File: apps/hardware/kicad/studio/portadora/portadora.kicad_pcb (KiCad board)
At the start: 2 copper layers, 0 parts

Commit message: feat(hardware): enclosure +15 mm, PCB-A de una cara y ubicación de la portadora
Enclosure (design/README.md, theory/02 §3 y §4.3–4.5), medido el módulo Freenove con la Pi:
- Cuña de 43/78 mm (+15 mm parejo, 12°): la portadora entra bajo la Pi con margen y hay más aire.
- Pantalla corrida 2.5 mm hacia atrás (centro y 114.9): el vidrio (120.8 × 76 × 7.6 mm) ya no se monta
  sobre PCB-K; ranuras de aire en y 155–165.
- Pi atornillada detrás de la Freenove, puertos hacia la derecha (adentro): se elimina la tapa de servicio.
- Jacks en una hilera baja soldados a la portadora (1/4" NRJ3HF-1); USB y palanca PAD de panel arriba.
  La placa trasera vertical se descartó antes de commit.

PCB-A: todos los SMD en la cara superior (ensamble Economic de una cara); vía propia para los GND del
JST; re-ruteada. DRC 0/0.

Portadora: tools/place_portadora.py (97 × 100 mm, jacks contra la pared, shield y entrada analógica al
medio, Teensy y alimentación adelante, J5/J6 al frente). DRC con paridad: 0 violaciones; falta rutear.
Herramientas: costura de GND que respeta agujeros e islas, route_board sin duplicar lo bloqueado,
sync_fp_fields con redes "unconnected" y atributos de BOM, trim_silk_outside.py.

Co-Authored-By: Claude Opus 5.5 <noreply@anthropic.com>
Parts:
- added C1: 100uF, Capacitor_SMD:CP_Elec_6.3x7.7, F.Cu at (178.0, 120.0)
- added C10: 10uF, Capacitor_SMD:C_0805_2012Metric, F.Cu at (185.0, 88.0)
- added C11: 10uF, Capacitor_SMD:C_0805_2012Metric, F.Cu at (147.0, 65.5)
- added C12: 10uF, Capacitor_SMD:C_0805_2012Metric, F.Cu at (129.0, 65.5)
- added C13: 100nF, Capacitor_SMD:C_0603_1608Metric, F.Cu at (103.0, 67.5)
- added C14: 100nF, Capacitor_SMD:C_0603_1608Metric, F.Cu at (107.0, 67.5)
- added C2: 100nF, Capacitor_SMD:C_0603_1608Metric, F.Cu at (148.0, 114.4)
- added C3: 10uF, Capacitor_SMD:C_0805_2012Metric, F.Cu at (171.0, 120.0)
- added C4: 100nF, Capacitor_SMD:C_0603_1608Metric, F.Cu at (186.0, 126.5)
- added C5: 1uF, Capacitor_SMD:C_0805_2012Metric, F.Cu at (150.0, 79.0)
- added C6: 1uF, Capacitor_SMD:C_0805_2012Metric, F.Cu at (150.0, 97.0)
- added C7: 100nF, Capacitor_SMD:C_0603_1608Metric, F.Cu at (168.0, 94.5)
- added C8: 2.2uF, Capacitor_SMD:C_0805_2012Metric, F.Cu at (176.0, 82.0)
- added C9: 2.2uF, Capacitor_SMD:C_0805_2012Metric, F.Cu at (176.0, 94.0)
- added D1: SMBJ5.0CA, Diode_SMD:D_SMB, F.Cu at (171.0, 112.0)
- added D2: BAT54S, Package_TO_SOT_SMD:SOT-23, F.Cu at (158.0, 79.0)
- added D3: BAT54S, Package_TO_SOT_SMD:SOT-23, F.Cu at (158.0, 97.0)
- added F1: 3A hold, Fuse:Fuse_1812_4532Metric, F.Cu at (177.0, 112.0)
- added J1: Teensy 4.1 izq, Connector_PinSocket_2.54mm:PinSocket_1x24_P2.54mm_Vertical, F.Cu at (101.3, 125.0)
- added J10: 5V desde USB-C de panel, Connector_JST:JST_XH_B2B-XH-A_1x02_P2.50mm_Vertical, F.Cu at (184.0, 112.0)
- added J11: OUT L 1/4 NRJ3HF-1, Connector_Audio:Jack_6.35mm_Neutrik_NRJ3HF-1_Horizontal, F.Cu at (139.8, 55.0)
- added J12: OUT R 1/4 NRJ3HF-1, Connector_Audio:Jack_6.35mm_Neutrik_NRJ3HF-1_Horizontal, F.Cu at (121.8, 55.0)
- added J13: PHONES 3.5 sleeve HP_VGND, Connector_Audio:Jack_3.5mm_CUI_SJ1-3533NG_Horizontal, F.Cu at (111.1, 39.2)
- added J14: CV OUT 3.5, Connector_Audio:Jack_3.5mm_CUI_SJ1-3533NG_Horizontal, F.Cu at (99.1, 39.2)
- added J15: Shield fila 13-5V, Connector_PinSocket_2.54mm:PinSocket_1x14_P2.54mm_Vertical, F.Cu at (106.5, 84.4)
- added J16: Shield fila 12-GND, Connector_PinSocket_2.54mm:PinSocket_1x14_P2.54mm_Vertical, F.Cu at (106.5, 99.6)
- added J2: Teensy 4.1 der, Connector_PinSocket_2.54mm:PinSocket_1x24_P2.54mm_Vertical, F.Cu at (101.3, 109.8)
- added J3: USB host Teensy, Connector_PinHeader_2.54mm:PinHeader_1x05_P2.54mm_Vertical, F.Cu at (96.5, 77.9)
- added J5: Panel IDC 2x15, Connector_IDC:IDC-Header_2x15_P2.54mm_Vertical, F.Cu at (144.2, 134.1)
- added J6: Raspberry Pi pines 1-10, Connector_IDC:IDC-Header_2x05_P2.54mm_Vertical, F.Cu at (101.9, 134.1)
- added J7: IN L 1/4 NRJ3HF-1, Connector_Audio:Jack_6.35mm_Neutrik_NRJ3HF-1_Horizontal, F.Cu at (175.8, 55.0)
- added J8: IN R 1/4 NRJ3HF-1, Connector_Audio:Jack_6.35mm_Neutrik_NRJ3HF-1_Horizontal, F.Cu at (157.8, 55.0)
- added J9: Audio Shield LINE y HP, Connector_PinHeader_2.54mm:PinHeader_1x09_P2.54mm_Vertical, F.Cu at (143.5, 83.6)
- added JP1: LED buffer o directo, Jumper:SolderJumper-3_P1.3mm_Bridged12_RoundedPad1.0x1.5mm, F.Cu at (153.0, 118.0)
- added JP2: BYP L (sin U2), Jumper:SolderJumper-2_P1.3mm_Open_RoundedPad1.0x1.5mm, F.Cu at (172.0, 78.5)
- added JP3: BYP R (sin U2), Jumper:SolderJumper-2_P1.3mm_Open_RoundedPad1.0x1.5mm, F.Cu at (172.0, 97.5)
- added JP4: BYP VREF (sin U2), Jumper:SolderJumper-2_P1.3mm_Open_RoundedPad1.0x1.5mm, F.Cu at (180.0, 96.0)
- added JP5: BYP CV (sin U2), Jumper:SolderJumper-2_P1.3mm_Open_RoundedPad1.0x1.5mm, F.Cu at (180.0, 80.0)
- added R10: 1k, Resistor_SMD:R_0603_1608Metric, F.Cu at (154.0, 79.0)
- added R11: 1k, Resistor_SMD:R_0603_1608Metric, F.Cu at (154.0, 97.0)
- added R12: 100k, Resistor_SMD:R_0603_1608Metric, F.Cu at (162.0, 79.0)
- added R13: 100k, Resistor_SMD:R_0603_1608Metric, F.Cu at (162.0, 97.0)
- added R14: 10k, Resistor_SMD:R_0603_1608Metric, F.Cu at (179.5, 88.0)
- added R15: 10k, Resistor_SMD:R_0603_1608Metric, F.Cu at (182.0, 88.0)
- added R16: 47k, Resistor_SMD:R_0603_1608Metric, F.Cu at (147.0, 68.5)
- added R17: 47k, Resistor_SMD:R_0603_1608Metric, F.Cu at (129.0, 68.5)
- added R18: 4.7k, Resistor_SMD:R_0603_1608Metric, F.Cu at (103.0, 65.0)
- added R19: 4.7k, Resistor_SMD:R_0603_1608Metric, F.Cu at (107.0, 65.0)
- added R20: 1k, Resistor_SMD:R_0603_1608Metric, F.Cu at (107.0, 70.0)
- added R3: 330, Resistor_SMD:R_0603_1608Metric, F.Cu at (157.0, 118.0)
- added R4: 32.4k, Resistor_SMD:R_0603_1608Metric, F.Cu at (183.0, 65.0)
- added R5: 12.4k, Resistor_SMD:R_0603_1608Metric, F.Cu at (183.0, 67.5)
- added R6: 5.23k, Resistor_SMD:R_0603_1608Metric, F.Cu at (183.0, 70.0)
- added R7: 32.4k, Resistor_SMD:R_0603_1608Metric, F.Cu at (165.0, 65.0)
- added R8: 12.4k, Resistor_SMD:R_0603_1608Metric, F.Cu at (165.0, 67.5)
- added R9: 5.23k, Resistor_SMD:R_0603_1608Metric, F.Cu at (165.0, 70.0)
- added SW1: PAD 0 -10 -20 dB, Connector_PinHeader_2.54mm:PinHeader_2x04_P2.54mm_Vertical, F.Cu at (172.7, 64.7)
- added TP1: VREF, TestPoint:TestPoint_Pad_D1.5mm, F.Cu at (187.0, 94.0)
- added TP2: BUF_L, TestPoint:TestPoint_Pad_D1.5mm, F.Cu at (187.0, 82.0)
- added TP3: BUF_R, TestPoint:TestPoint_Pad_D1.5mm, F.Cu at (187.0, 100.0)
- added TP4: CV_BUF, TestPoint:TestPoint_Pad_D1.5mm, F.Cu at (187.0, 76.0)
- added TP5: GND, TestPoint:TestPoint_Pad_D1.5mm, F.Cu at (147.8, 88.0)
- added U1: 74AHCT1G125, Package_TO_SOT_SMD:SOT-23-5, F.Cu at (148.0, 118.0)
- added U2: MCP6004, Package_SO:SOIC-14_3.9x8.7mm_P1.27mm, F.Cu at (168.0, 88.0)
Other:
- board outline added: 97 x 100 mm

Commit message: feat(hardware): portadora ruteada (DRC limpio) y pinout del IDC reordenado
- Portadora: ruteo completo, DRC con paridad de esquemático 0/0/0 contra reglas de JLCPCB.
  +5V de F1 a la Pi en ~40 mm con una vía; sin paralelos audio↔digital a <1 mm.
- IDC 2×15 (PCB-A J2 ↔ portadora J5): pines ordenados por la X del pin de la Teensy al que van,
  para que el bus salga del conector sin cruces. Ambos esquemáticos re-etiquetados (ERC limpio),
  PCB-A re-ruteada (DRC 0/0/0). Tablas y razón en theory/02 §6.2.
- Herramientas: grid_route (Dijkstra en grilla 0.1 mm, 2 capas), finish_routing (rip-up and
  reroute de lo que deja Freerouting), clean_vias, add_gnd_escapes, fix_portadora_gnd,
  set_idc_pinout y build_portadora.sh (pipeline completo reproducible).

Co-Authored-By: Claude Opus 5.5 <noreply@anthropic.com>
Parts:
- moved J10 65.6 mm to (122.0, 133.5)
- moved C3 51.2 mm to (120.5, 128.4), turned to 0 degrees
- moved F1 50.2 mm to (132.5, 135.2), turned to 0 degrees
- moved D1 42.4 mm to (132.8, 130.4), turned to 0 degrees
- moved C1 2.00 mm to (178.0, 118.0)
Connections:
- J5 pad 11: /B5 -> /NAV_B
- J5 pad 12: /B6 -> /NAV_A
- J5 pad 13: /ENCL_A -> /P2_SW
- J5 pad 14: /ENCL_B -> /ENCR_SW
- J5 pad 15: /ENCL_SW -> /ENCL_A
- J5 pad 16: /ENCR_A -> /ENCR_B
- J5 pad 17: /ENCR_B -> /ENCL_B
- J5 pad 18: /ENCR_SW -> /ENCR_A
- J5 pad 19: /NAV_A -> /ENCL_SW
- J5 pad 20: /NAV_B -> /B6
- J5 pad 21: /NAV_SW -> /POT_IN
- J5 pad 22: /P1_A -> /B5
- J5 pad 23: /P1_B -> /NAV_SW
- J5 pad 24: /P1_SW -> /P2_B
- J5 pad 25: /P2_A -> /P1_A
- J5 pad 26: /P2_B -> /LED_DIN
- J5 pad 27: /P2_SW -> /P2_A
- J5 pad 28: /POT_IN -> /P1_B
- J5 pad 29: /POT_VOL -> /P1_SW
- J5 pad 5: /LED_DIN -> /B1
- J5 pad 7: /B1 -> /B2
- J5 pad 8: /B2 -> /POT_VOL
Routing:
- net /+3V3: track 0.00 -> 200.0 mm, vias 0 -> 2
- net /+5V: track 0.00 -> 164.2 mm, vias 0 -> 3
- net /CV_BUF: track 0.00 -> 105.6 mm, vias 0 -> 2
- net /GND: track 0.00 -> 104.8 mm, vias 0 -> 153
- net /CV_FILT: track 0.00 -> 93.6 mm, vias 0 -> 2
- net /CV_PWM: track 0.00 -> 92.5 mm, vias 0 -> 1
- net /HP_VGND: track 0.00 -> 79.0 mm
- net /P1_A: track 0.00 -> 78.4 mm, vias 0 -> 2
- net /POT_VOL: track 0.00 -> 76.2 mm, vias 0 -> 5
- net /P2_SW: track 0.00 -> 71.1 mm, vias 0 -> 2
- net /HP_L: track 0.00 -> 69.9 mm
- net /VREF: track 0.00 -> 68.3 mm, vias 0 -> 3
- net /HP_R: track 0.00 -> 66.9 mm
- net /NAV_SW: track 0.00 -> 54.0 mm
- net /NAV_B: track 0.00 -> 51.4 mm, vias 0 -> 2
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- added copper zone on B.Cu, net /GND
- added copper zone on F.Cu, net /GND

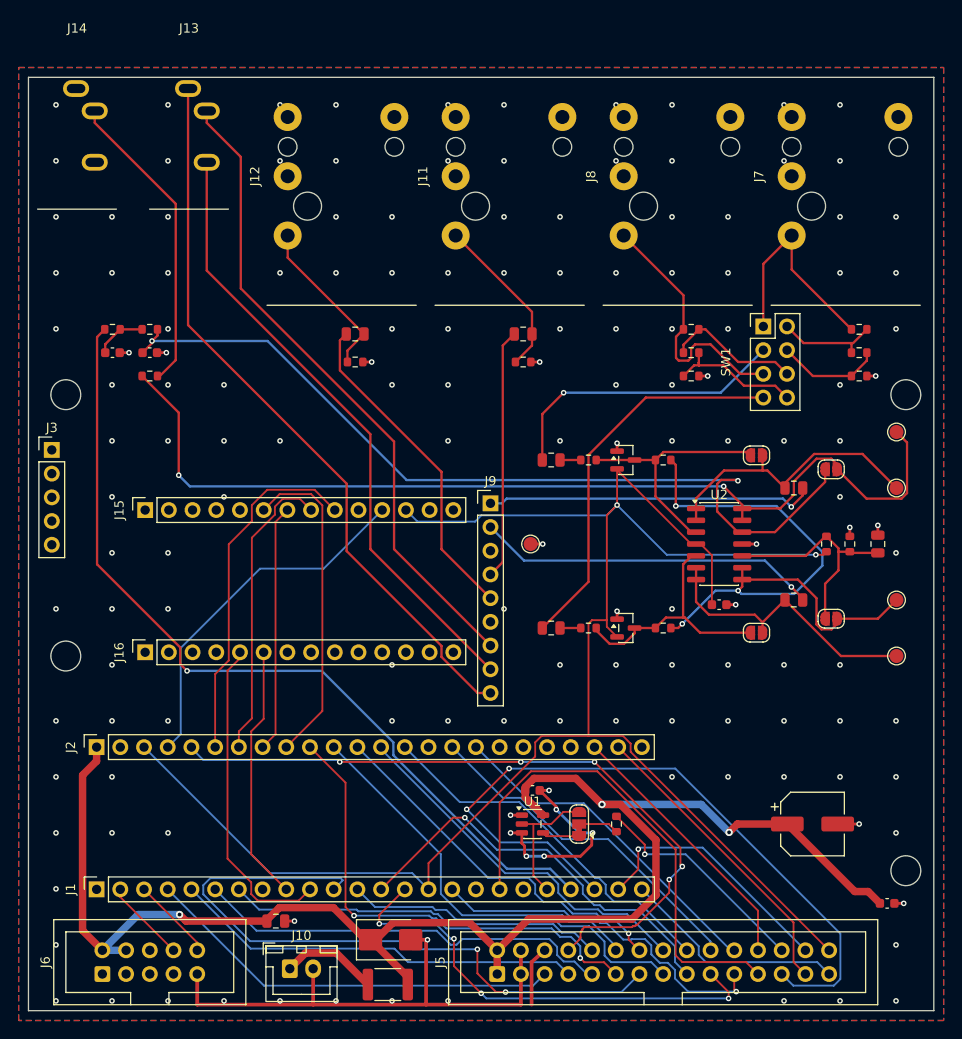
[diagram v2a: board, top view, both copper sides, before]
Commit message: feat(hardware): archivos de fabricación JLCPCB y shield corregido en la portadora
- Portadora: las filas del Audio Shield estaban al revés (quedaba espejado respecto de la Teensy con el
  shield boca arriba). J16 (GND/0–12) pasa atrás y J15 adelante; re-ruteada, DRC con paridad 0/0/0.
- Números LCSC en los tres esquemáticos (set_lcsc.py), todo en ensamble Economic. PCB-K pasa al
  SK6812MINI-EA (mismo pinout y cuerpo, sin la restricción Standard-only del MINI-E).
- Escalera del PAD y acople al codec con valores Basic (33k/12k/5.1k, 4.7 µF): la simulación sigue
  pasando C1–C6 (tercera corrida en theory/03).
- export_fab.py: Gerbers + taladros, BOM y CPL en formato JLC; los THT usan el centro de sus pads y los
  IDC la rotación del modelo de JLC. Portadora con jacks e IDC ensamblados; el resto de los THT en
  fab/lcsc-piezas-sueltas.csv.
- sync_fp_fields.py también copia Value y LCSC a las placas.
- theory/02 §10C–10D: fabricación, montaje del shield, J9, J3 (USB host), corriente de la Pi y la
  verificación de punta a punta de las conexiones.

Co-Authored-By: Claude Opus 5.5 <noreply@anthropic.com>
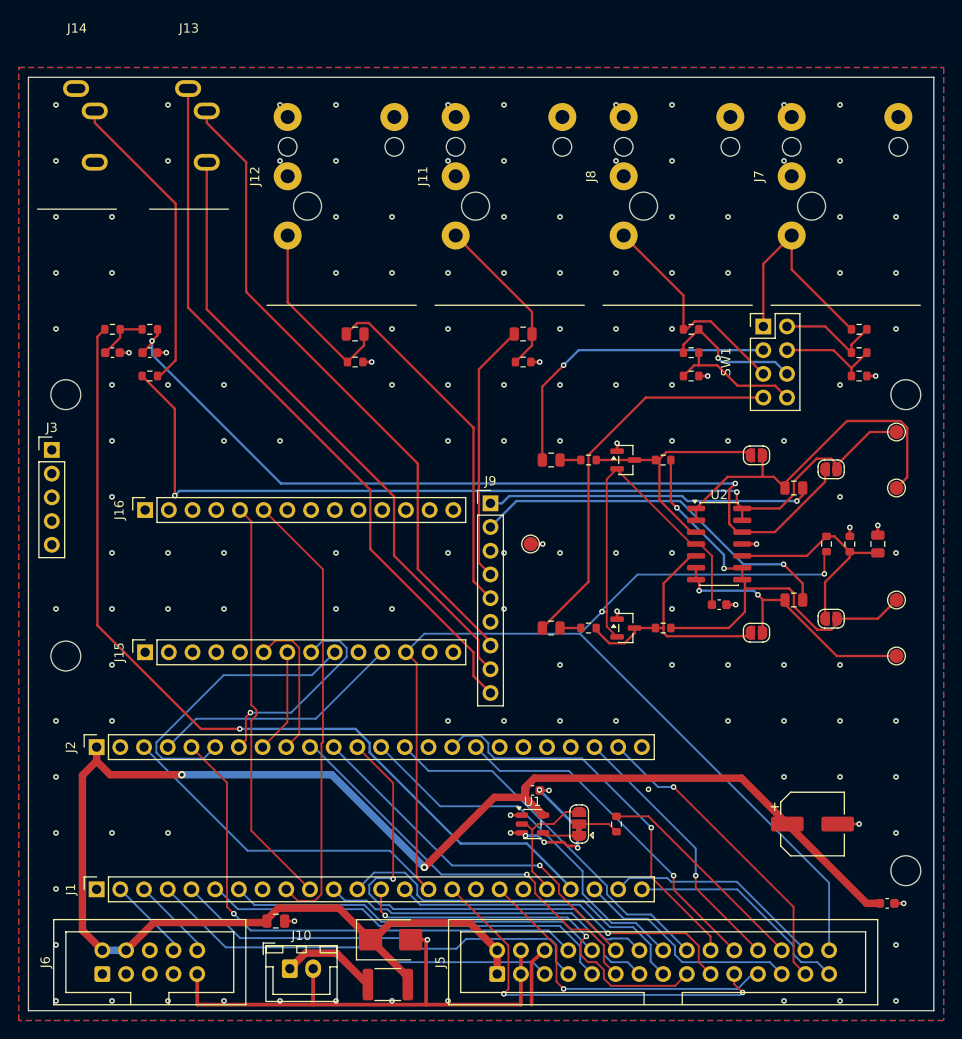
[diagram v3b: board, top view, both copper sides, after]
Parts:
- C8, C9: value 2.2uF -> 4.7uF
- R4, R7: value 32.4k -> 33k
- R5, R8: value 12.4k -> 12k
- R6, R9: value 5.23k -> 5.1k
- moved J15 15.2 mm to (106.5, 99.6)
- moved J16 15.2 mm to (106.5, 84.4)
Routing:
- net /P1_A: track 78.4 -> 24.4 mm, vias 2 -> 0
- net /P2_SW: track 71.1 -> 37.1 mm, vias 2 -> 0
- net /I2S_TX: track 27.5 -> 48.4 mm
- net /I2C_SDA: track 35.0 -> 15.9 mm
- net /POT_VOL: track 76.2 -> 57.2 mm, vias 5 -> 1
- net /NAV_SW: track 54.0 -> 35.0 mm, vias 0 -> 1
- net /VREF: track 68.3 -> 50.0 mm, vias 3 -> 2
- net /+5V: track 164.2 -> 182.2 mm, vias 3 -> 2
- net /I2C_SCL: track 26.5 -> 11.3 mm
- net /ENCL_SW: track 50.7 -> 37.5 mm, vias 4 -> 1
- net /I2S_MCLK: track 38.9 -> 27.2 mm
- net /ENCR_SW: track 40.2 -> 51.1 mm
- net /I2S_RX: track 34.6 -> 44.2 mm
- net /I2S_LRCLK: track 32.1 -> 22.6 mm, vias 0 -> 1
- net /BUF_L: track 30.8 -> 38.6 mm
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
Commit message: fix(studio): ENC R-A pasa del pin 13 al pin 6 (auditoría de fabricación F1)
El pin 13 de la Teensy 4.1 tiene el LED con 470 Ω a GND: con el INPUT_PULLUP de Encoder la
fase A puede no llegar a HIGH. Aprobado por Juan: pin 6, el único que 01 §3.3 no reserva
(en Studio es el MEMCS del shield, que no se cablea). 01 §3.3 enmendado; portadora:
etiqueta ENCR_A en J1.8 y solo esa red re-ruteada (J5.18 → J1.8), DRC 0 / paridad 0 /
ERC 0 errores; gerbers regenerados (BOM y CPL sin cambios). Firmware: enc_r(6, 14).

Co-Authored-By: Claude Opus 5.5 <noreply@anthropic.com>
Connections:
- J1 pad 8: unconnected-(J1-Pin_8-Pad8) -> /ENCR_A
- J2 pad 14: /ENCR_A -> unconnected-(J2-Pin_14-Pad14)
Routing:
- net /ENCR_A: track 39.8 -> 63.7 mm, vias 0 -> 6

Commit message: fix(portadora): vías fuera de los pads, retorno del I2S cosido, C7 junto a U2 y C4 lejos del agujero
Auditoría delta D04/D05/D06/D08, cambios locales sin re-rutear la placa:
- D05: las vías en C2.2 y U1.3 (del ruteo de grilla) se reemplazan por pistas desde sus
  vías de escape. check_via_in_pad.py: 2 → 0.
- D06: C7 a la izquierda de U2.4; pista U2.4 → C7 de 7.45 a 2.05 mm.
- D08: C4 a (179.5, 125.5): cuerpo a 6.1 mm del borde del agujero (antes ~1.7).
- D04: stitch_returns.py pone GND a 0.90 mm de la vía de LRCLK (antes 11.47) y vías en
  los huecos del plano a lo largo del bus: tramo más largo sin plano opuesto MCLK
  12.8 → 2.1 mm, BCLK 9.5 → 2.4, LRCLK 8.4 → 1.8, TX 16.1 → 4.1, RX 11.3 → 6.1.
DRC 0 / sin conectar 0 / paridad 0. Gerbers y CPL regenerados (BOM sin cambios).
Pipeline: posiciones nuevas en place_portadora.py, costura y control de vías en pads.

Co-Authored-By: Claude Opus 5.5 <noreply@anthropic.com>
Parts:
- moved C7 8.39 mm to (162.7, 88.0), turned to 180 degrees
- moved C4 6.58 mm to (179.5, 125.5)
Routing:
- net /+3V3: track 197.8 -> 192.3 mm
- net /+5V: track 182.2 -> 177.7 mm
- net /GND: track 100.1 -> 101.6 mm, vias 151 -> 287
